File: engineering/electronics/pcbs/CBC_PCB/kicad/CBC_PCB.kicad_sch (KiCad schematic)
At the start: 0 parts

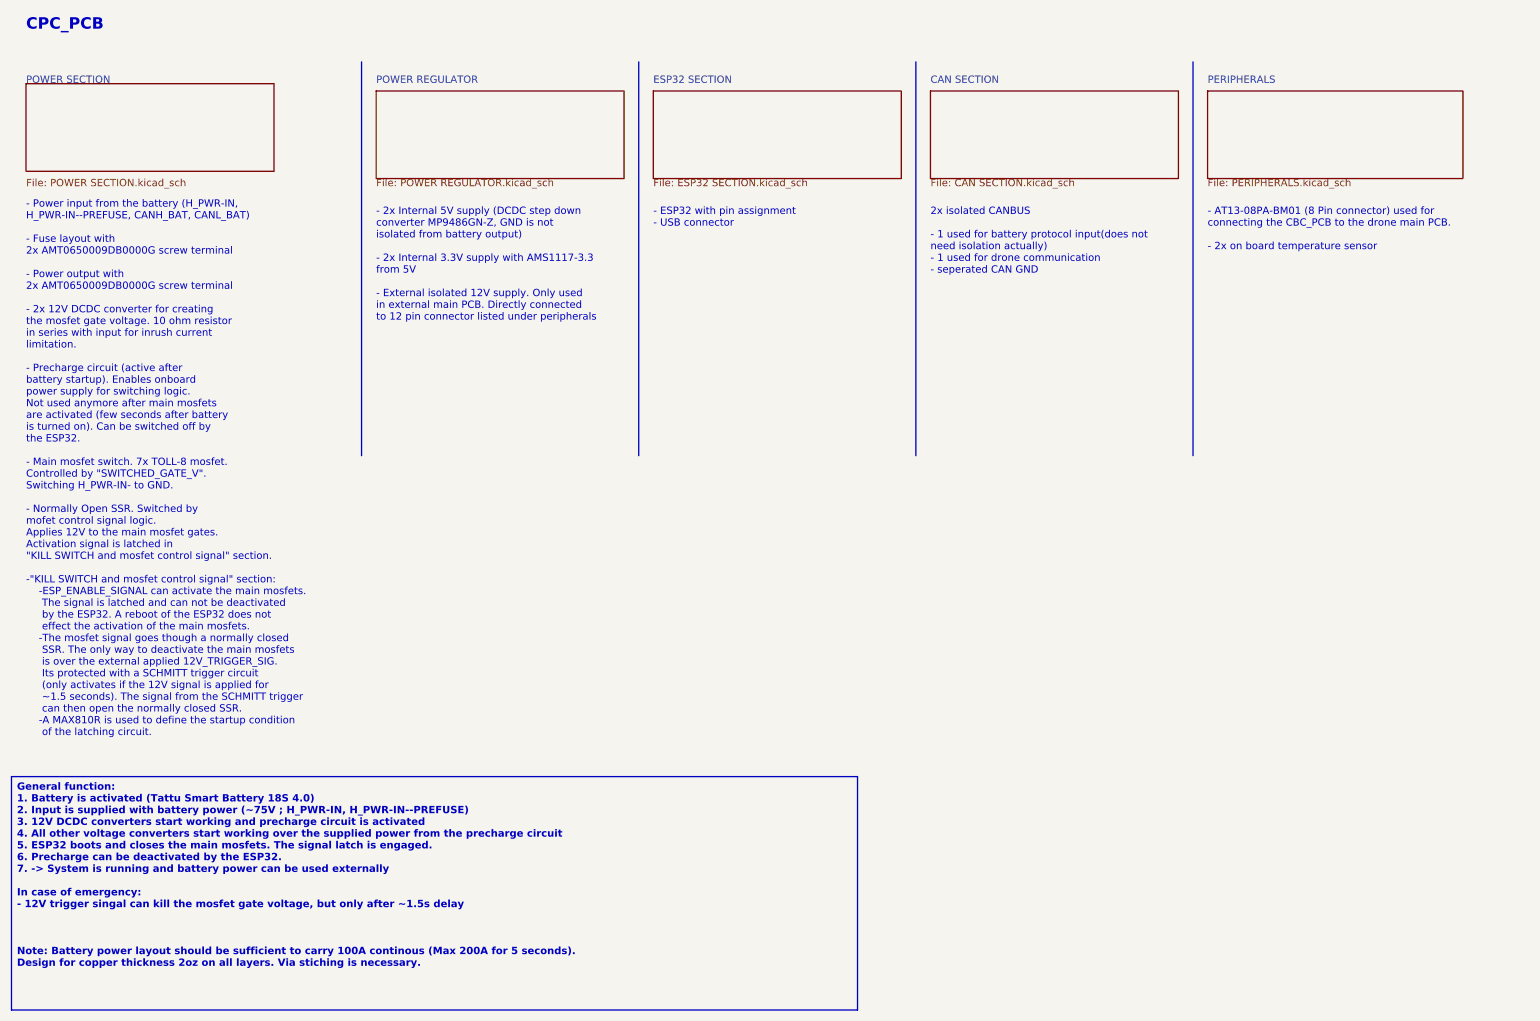
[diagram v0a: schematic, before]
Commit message: feat(cbc): integrate PT1.5 CBC PCB update for the US build
Julius's CPC_PCB_21_10_26_5 package (issue #58): precharge ground fix with the new H_PWR-OUT- net and NT201, precharge and HV bus sensing, BZ501 buzzer, aux input inrush limiting (RT601, R628/R629, F604), BOM-review part swaps, and JLC production outputs. The board STEP is zipped because the raw export is 127 MB, which is over GitHub's 100 MB file limit.
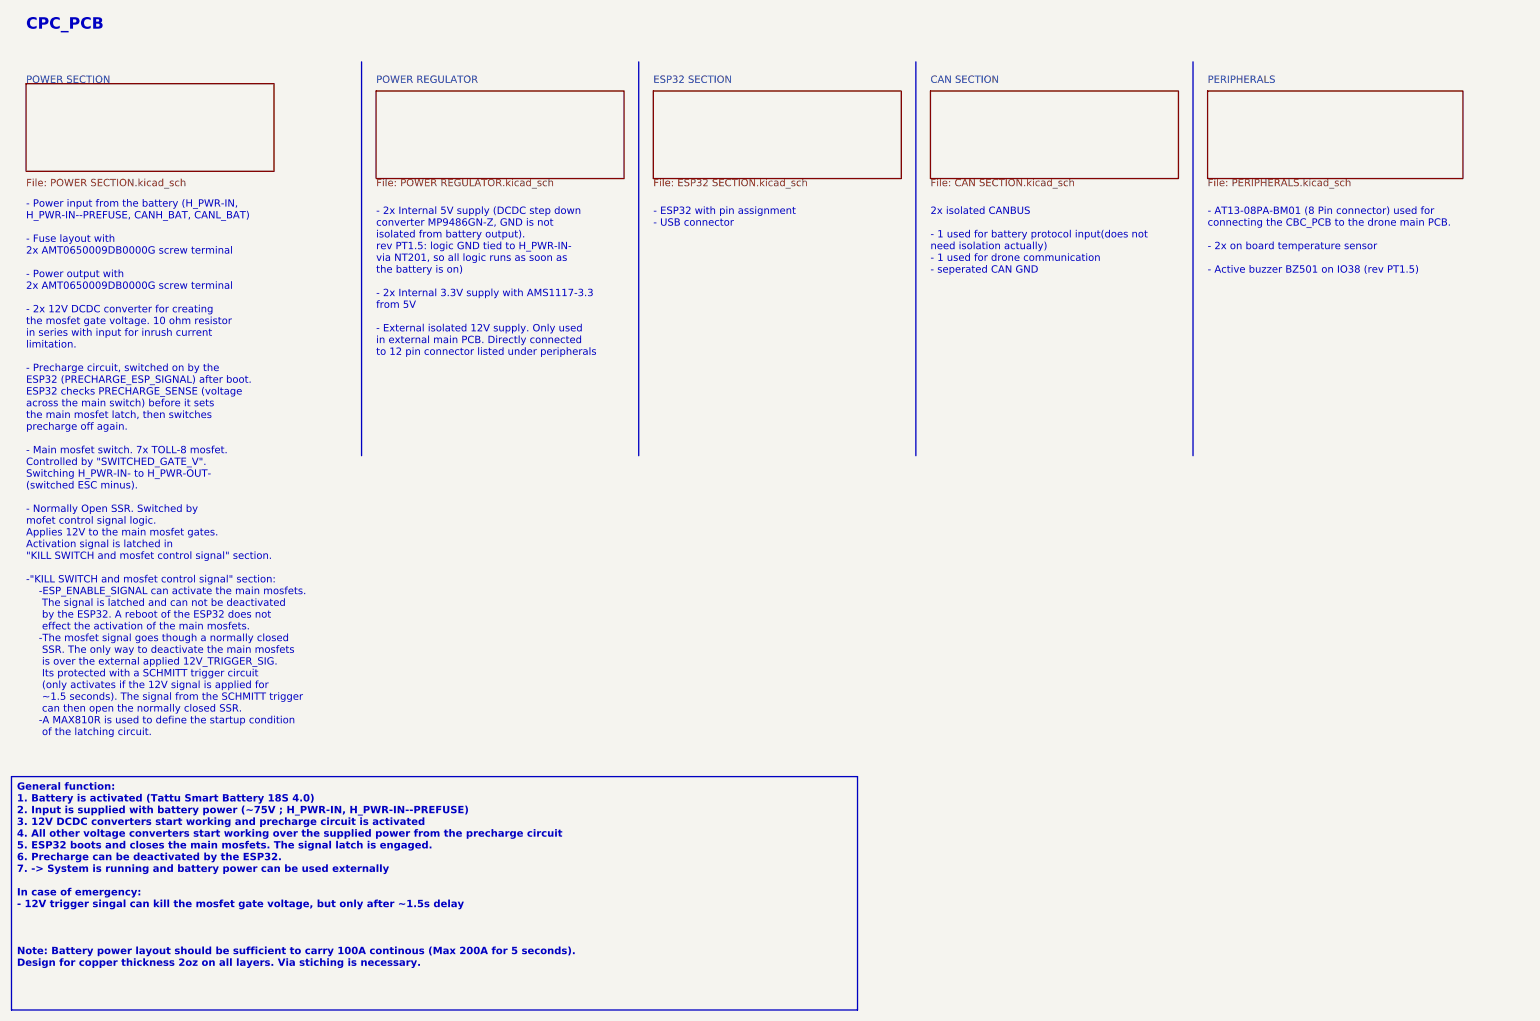
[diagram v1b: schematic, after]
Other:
- note added: "- 2x Internal 5V supply (DCDC step down converter MP9486GN-Z, GND is not isolated from battery output). rev PT1.5: logic GND tied to H_PWR-IN- via NT201, so all logic runs as soon as the battery is on) - 2x Internal 3.3V supply with AMS1117-3.3 from 5V - External isolated 12V supply. Only used in external main PCB. Directly connected to 12 pin connector listed under peripherals"
- note added: "- AT13-08PA-BM01 (8 Pin connector) used for connecting the CBC_PCB to the drone main PCB. - 2x on board temperature sensor - Active buzzer BZ501 on IO38 (rev PT1.5)"
- note added: "- Power input from the battery (H_PWR-IN, H_PWR-IN--PREFUSE, CANH_BAT, CANL_BAT) - Fuse layout with 2x AMT0650009DB0000G screw terminal - Power output with 2x AMT0650009DB0000G screw terminal - 2x 12V DCDC converter for creating the mosfet gate voltage. 10 ohm resistor in series with input for inrush current limitation. - Precharge circuit, switched on by the ESP32 (PRECHARGE_ESP_SIGNAL) after bo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"
- note removed: "- 2x Internal 5V supply (DCDC step down converter MP9486GN-Z, GND is not isolated from battery output) - 2x Internal 3.3V supply with AMS1117-3.3 from 5V - External isolated 12V supply. Only used in external main PCB. Directly connected to 12 pin connector listed under peripherals"
- note removed: "- AT13-08PA-BM01 (8 Pin connector) used for connecting the CBC_PCB to the drone main PCB. - 2x on board temperature sensor"
- note removed: "- Power input from the battery (H_PWR-IN, H_PWR-IN--PREFUSE, CANH_BAT, CANL_BAT) - Fuse layout with 2x AMT0650009DB0000G screw terminal - Power output with 2x AMT0650009DB0000G screw terminal - 2x 12V DCDC converter for creating the mosfet gate voltage. 10 ohm resistor in series with input for inrush current limitation. - Precharge circuit (active after battery startup). Enables onboard power sup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"
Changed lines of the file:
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@@
 	(generator_version "10.0")
 	(paper "A4")
-	(text "- 2x Internal 5V supply (DCDC step down\nconverter MP9486GN-Z, GND is not\nisolated from battery output)\n\n- 2x Internal 3.3V supply with AMS1117-3.3\nfrom 5V\n\n- External isolated 12V supply. Only used\nin external main PCB. Directly connected\nto 12 pin connector listed under peripherals "
+	(text "- 2x Internal 5V supply (DCDC step down\nconverter MP9486GN-Z, GND is not\nisolated from battery output).\nrev PT1.5: logic GND tied to H_PWR-IN-\nvia NT201, so all logic runs as soon as\nthe battery is on)\n\n- 2x Internal 3.3V supply with AMS1117-3.3\nfrom 5V\n\n- External isolated 12V supply. Only used\nin external main PCB. Directly connected\nto 12 pin connector listed under peripherals "
 		(exclude_from_sim no)
 		(at 86.36 50.8 0)
@@
 		)
 	)
-	(text "- Power input from the battery (H_PWR-IN,\nH_PWR-IN--PREFUSE, CANH_BAT, CANL_BAT)\n\n- Fuse layout with\n2x AMT0650009DB0000G screw terminal\n\n- Power output with\n2x AMT0650009DB0000G screw terminal\n\n- 2x 12V DCDC converter for creating\nthe mosfet gate voltage. 10 ohm resistor\nin series with input for inrush current\nlimitation.\n\n- Precharge circuit (active after\nbattery startup). Enables onboard\npower supply for switching logic.\nNot used anymore after main mosfets\nare activated (few seconds after battery\nis turned on). Can be switched off by\nthe ESP32.\n\n- Main mosfet switch. 7x TOLL-8 mosfet.\nControlled by \"SWITCHED_GATE_V\".\nSwitching H_PWR-IN- to GND.\n\n- Normally Open SSR. Switched by\nmofet control signal logic.\nApplies 12V to the main mosfet gates.\nActivation signal is latched in\n\"KILL SWITCH and mosfet control signal\" section.\n\n-\"KILL SWITCH and mosfet control signal\" section:\n	-ESP_ENABLE_SIGNAL can activate the main mosfets.\n	 The signal is latched and can not be deactivated\n	 by the ESP32. A reboot of the ESP32 does not\n	 effect the activation of the main mosfets.\n	-The mosfet signal goes though a normally closed\n	 SSR. The only way to deactivate the main mosfets\n	 is over the external applied 12V_TRIGGER_SIG.\n	 Its protected with a SCHMITT trigger circuit\n	 (only activates if the 12V signal is applied for\n	 ~1.5 seconds). The signal from the SCHMITT trigger\n	 can then open the normally closed SSR.\n	-A MAX810R is used to define the startup condition\n	 of the latching circuit.\n\n"
+	(text "- Power input from the battery (H_PWR-IN,\nH_PWR-IN--PREFUSE, CANH_BAT, CANL_BAT)\n\n- Fuse layout with\n2x AMT0650009DB0000G screw terminal\n\n- Power output with\n2x AMT0650009DB0000G screw terminal\n\n- 2x 12V DCDC converter for creating\nthe mosfet gate voltage. 10 ohm resistor\nin series with input for inrush current\nlimitation.\n\n- Precharge circuit, switched on by the\nESP32 (PRECHARGE_ESP_SIGNAL) after boot.\nESP32 checks PRECHARGE_SENSE (voltage\nacross the main switch) before it sets\nthe main mosfet latch, then switches\nprecharge off again.\n\n- Main mosfet switch. 7x TOLL-8 mosfet.\nControlled by \"SWITCHED_GATE_V\".\nSwitching H_PWR-IN- to H_PWR-OUT-\n(switched ESC minus).\n\n- Normally Open SSR. Switched by\nmofet control signal logic.\nApplies 12V to the main mosfet gates.\nActivation signal is latched in\n\"KILL SWITCH and mosfet control signal\" section.\n\n-\"KILL SWITCH and mosfet control signal\" section:\n	-ESP_ENABLE_SIGNAL can activate the main mosfets.\n	 The signal is latched and can not be deactivated\n	 by the ESP32. A reboot of the ESP32 does not\n	 effect the activation of the main mosfets.\n	-The mosfet signal goes though a normally closed\n	 SSR. The only way to deactivate the main mosfets\n	 is over the external applied 12V_TRIGGER_SIG.\n	 Its protected with a SCHMITT trigger circuit\n	 (only activates if the 12V signal is applied for\n	 ~1.5 seconds). The signal from the SCHMITT trigger\n	 can then open the normally closed SSR.\n	-A MAX810R is used to define the startup condition\n	 of the latching circuit.\n\n"
 		(exclude_from_sim no)
 		(at 25.4 49.53 0)
@@
 		)
 	)
-	(text "- AT13-08PA-BM01 (8 Pin connector) used for\nconnecting the CBC_PCB to the drone main PCB.\n\n- 2x on board temperature sensor"
+	(text "- AT13-08PA-BM01 (8 Pin connector) used for\nconnecting the CBC_PCB to the drone main PCB.\n\n- 2x on board temperature sensor\n\n- Active buzzer BZ501 on IO38 (rev PT1.5)"
 		(exclude_from_sim no)
 		(at 231.14 50.8 0)
